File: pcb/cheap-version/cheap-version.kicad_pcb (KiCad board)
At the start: 4 copper layers, 100 x 100 mm, 169 parts, among them J201 UART / 3V3 logic, J301 SHT4x / XH 2.50, J302 FLOAT / 3.5 mm, J401 HRO TF-01A, J501 FAN1 / 3.5 mm, J511 FAN2 / 3.5 mm, J521 PUMP 24V / 6W, J601 PTC + / switched - (3.5 mm), J711 LED +/- (return isolated), J721 LED +/- (return isolated), J731 LED +/- (return isolated), J901 24V IN (KF301-5.0-2P), Q501 AO3400A, Q511 AO3400A, Q521 AO3422, Q601 IRL2505, Q711 BSC146N10LS5, Q721 BSC146N10LS5, SW201 RESET, SW202 BOOT, U101 ST1S10PHR, U201 ESP32-WROOM-32E-N4, U301 PCF8563T/5, U601 IRS4427S, U700 SN74LVC1G08DBVR, U710 AL8853S-13, U720 AL8853S-13, U902 ST1S14PHR, Y301 32.768k 12.5pF

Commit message: Complete cheap-version connections and load project routing rules
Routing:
- net +24V_LOADS: track 54.0 -> 74.8 mm, vias 0 -> 2
- net /LEDDrivers/LED2_OUT: track 87.8 -> 102.1 mm, vias 1 -> 3
- net +3V3: track 226.9 -> 238.9 mm, vias 2 -> 4
- net /LEDDrivers/LED2_GATE: track 1.78 -> 12.2 mm
- net /LEDDrivers/LED1_RETURN: track 0.00 -> 8.91 mm
- net /InputPower/AUX_VIN: track 37.8 -> 44.7 mm, vias 3 -> 5
- net /LEDDrivers/LED1_GATE: track 2.35 -> 8.55 mm, vias 0 -> 2
- net /LEDDrivers/LED2_OVP: track 6.29 -> 9.98 mm, vias 0 -> 2
- added copper zone on In2.Cu, net +3V3
- added copper zone on B.Cu, net GND
- added copper zone on F.Cu, net GND

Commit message: Reinforce cheap-version input and heater copper
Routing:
- net +24V_LOADS: track 74.8 -> 22.7 mm
- net GND: vias 99 -> 103
- added copper zone on B.Cu, net +24V
- added copper zone on F.Cu, net +24V
- added copper zone on B.Cu, net +24V_LOADS
- added copper zone on B.Cu, net /Outputs/Heater/HEATER_DRAIN
- added copper zone on F.Cu, net /Outputs/Heater/HEATER_DRAIN
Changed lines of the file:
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@@
 			(roundrect_rratio 0.032051)
 			(net "+24V")
+			(zone_connect 2)
 		)
 		(pad "2" smd roundrect
@@
 			(roundrect_rratio 0.104167)
 			(net "+24V_LOADS")
+			(zone_connect 2)
 		)
 		(pad "2" thru_hole circle
@@
 			(remove_unused_layers no)
 			(net "/Outputs/Heater/HEATER_DRAIN")
+			(zone_connect 2)
 		)
 		(embedded_fonts no)
@@
 			(roundrect_rratio 0.25)
 			(net "+24V")
+			(zone_connect 2)
 		)
 		(pad "1" thru_hole circle
@@
 			(remove_unused_layers no)
 			(net "+24V")
+			(zone_connect 2)
 		)
 		(pad "2" thru_hole circle
@@
 			(remove_unused_layers no)
 			(net "+24V_LOADS")
+			(zone_connect 2)
 		)
 		(pad "2" thru_hole circle
@@
 			(remove_unused_layers no)
 			(net "+24V_LOADS")
+			(zone_connect 2)
 		)
 		(embedded_fonts no)
@@
 	)
 	(via
+		(at 61.5 82.5)
+		(size 0.8)
+		(drill 0.4)
+		(layers "F.Cu" "B.Cu")
+		(locked yes)
+		(net "GND")
+	)
+	(via
 		(at 80.865 91.425)
 		(size 0.65)
@@
 	)
 	(via
+		(at 60.5 80.5)
+		(size 0.8)
+		(drill 0.4)
+		(layers "F.Cu" "B.Cu")
+		(locked yes)
+		(net "GND")
+	)
+	(via
 		(at 104.941267 118.220951)
 		(size 0.65)
@@
 	)
 	(via
+		(at 60.5 81.5)
+		(size 0.8)
+		(drill 0.4)
+		(layers "F.Cu" "B.Cu")
+		(locked yes)
+		(net "GND")
+	)
+	(via
 		(at 85.1125 80.25)
 		(size 0.65)
@@
 	)
 	(via
+		(at 60.5 82.5)
+		(size 0.8)
+		(drill 0.4)
+		(layers "F.Cu" "B.Cu")
+		(locked yes)
+		(net "GND")
+	)
+	(via
 		(at 131.174999 78.8)
 		(size 0.65)
@@
 	)
 	(segment
-		(start 61.1 82.9)
-		(end 60.8 82.6)
-		(width 1)
-		(locked yes)
-		(layer "B.Cu")
-		(net "+24V_LOADS")
-	)
-	(segment
-		(start 66.099999 82.9)
-		(end 61.1 82.9)
-		(width 1)
-		(locked yes)
-		(layer "B.Cu")
-		(net "+24V_LOADS")
-	)
-	(segment
-		(start 67.2 84)
-		(end 66.099999 82.9)
-		(width 1)
-		(locked yes)
-		(layer "B.Cu")
-		(net "+24V_LOADS")
-	)
-	(segment
-		(start 60.8 82.6)
-		(end 60.7 82.6)
+		(start 69.5 77)
+		(end 69.5 81.7)
 		(width 1)
 		(locked yes)
@@
 	)
 	(segment
-		(start 60.7 82.6)
-		(end 56.1 78)
+		(start 69.5 81.7)
+		(end 67.2 84)
 		(width 1)
 		(locked yes)
@@
 	)
 	(segment
-		(start 56.2589 75.8411)
-		(end 73.5589 75.8411)
-		(width 3)
-		(layer "In2.Cu")
-		(net "+24V_LOADS")
-	)
-	(segment
-		(start 89.65 59.75)
-		(end 89.65 56.35)
-		(width 3)
-		(layer "In2.Cu")
-		(net "+24V_LOADS")
-	)
-	(segment
-		(start 73.5589 75.8411)
-		(end 89.65 59.75)
-		(width 3)
-		(layer "In2.Cu")
-		(net "+24V_LOADS")
-	)
-	(segment
-		(start 54.1 78)
-		(end 56.2589 75.8411)
-		(width 3)
-		(layer "In2.Cu")
-		(net "+24V_LOADS")
-	)
-	(segment
 		(start 146.5 134.54)
 		(end 141.965 134.54)
@@
 	)
 	(zone
+		(net "+24V")
+		(layer "F.Cu")
+		(name "auto:input-stage:input top")
+		(hatch edge 0.5)
+		(priority 10)
+		(connect_pads yes
+			(clearance 0)
+		)
+		(min_thickness 0.25)
+		(fill yes
+			(thermal_gap 0.4)
+			(thermal_bridge_width 0.5)
+			(island_removal_mode 0)
+		)
+		(polygon
+			(pts
+				(xy 52 51) (xy 84 51) (xy 84 76) (xy 75 76) (xy 75 65) (xy 70.5 65) (xy 70.5 61) (xy 52 61)
+			)
+		)
+	)
+	(zone
 		(net "GND")
 		(layer "F.Cu")
@@
 	)
 	(zone
+		(net "/Outputs/Heater/HEATER_DRAIN")
+		(layer "F.Cu")
+		(name "auto:input-stage:heater top")
+		(hatch edge 0.5)
+		(priority 10)
+		(connect_pads yes
+			(clearance 0)
+		)
+		(min_thickness 0.25)
+		(fill yes
+			(thermal_gap 0.4)
+			(thermal_bridge_width 0.5)
+			(island_removal_mode 0)
+		)
+		(polygon
+			(pts
+				(xy 51.5 80) (xy 55.5 80) (xy 59.5 84) (xy 62 84) (xy 63.5 80) (xy 65.4 80) (xy 66.4 83) (xy 66.4 87.8)
+				(xy 58 87.8) (xy 51.5 82)
+			)
+		)
+	)
+	(zone
+		(net "/Outputs/Heater/HEATER_DRAIN")
+		(layer "B.Cu")
+		(name "auto:input-stage:heater bottom")
+		(hatch edge 0.5)
+		(priority 10)
+		(connect_pads yes
+			(clearance 0)
+		)
+		(min_thickness 0.25)
+		(fill yes
+			(thermal_gap 0.4)
+			(thermal_bridge_width 0.5)
+			(island_removal_mode 0)
+		)
+		(polygon
+			(pts
+				(xy 51.5 80) (xy 55.5 80) (xy 59.5 84) (xy 62 84) (xy 63.5 80) (xy 65.4 80) (xy 66.4 83) (xy 66.4 87.8)
+				(xy 58 87.8) (xy 51.5 82)
+			)
+		)
+	)
+	(zone
+		(net "+24V")
+		(layer "B.Cu")
+		(name "auto:input-stage:input bottom")
+		(hatch edge 0.5)
+		(priority 10)
+		(connect_pads yes
+			(clearance 0)
+		)
+		(min_thickness 0.25)
+		(fill yes
+			(thermal_gap 0.4)
+			(thermal_bridge_width 0.5)
+			(island_removal_mode 0)
+		)
+		(polygon
+			(pts
+				(xy 52 51) (xy 84 51) (xy 84 61.5) (xy 52 61.5)
+			)
+		)
+	)
+	(zone
 		(net "GND")
 		(layer "B.Cu")
@@
 			)
 		)
+	)
+	(zone
+		(net "+24V_LOADS")
+		(layer "B.Cu")
+		(name "auto:input-stage:loads bottom")
+		(hatch edge 0.5)
+		(priority 10)
+		(connect_pads yes
+			(clearance 0)
+		)
+		(min_thickness 0.25)
+		(fill yes
+			(thermal_gap 0.4)
+			(thermal_bridge_width 0.5)
+			(island_removal_mode 0)
+		)
+		(polygon
+			(pts
+				(xy 86.5 53) (xy 93 53) (xy 93 64) (xy 77.7 79.3) (xy 51.5 79.3) (xy 51.5 72.8) (xy 75 72.8) (xy 86.5 61.3)
+			)
+		)

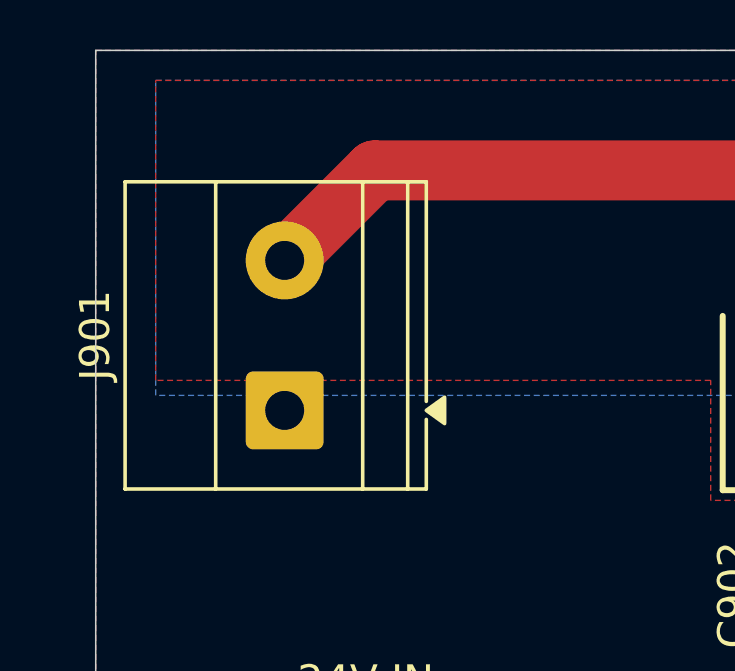
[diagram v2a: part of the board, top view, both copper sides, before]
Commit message: Turn 24V input terminal toward board edge preserving polarity
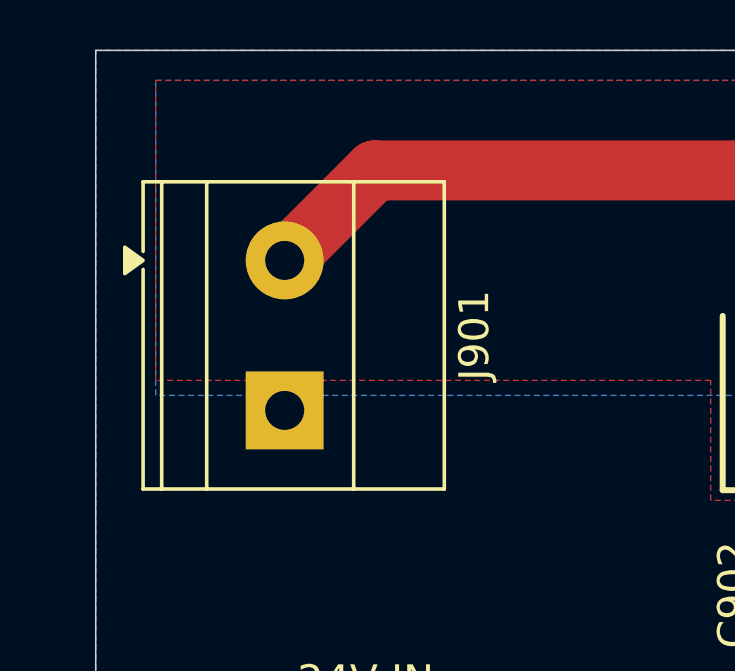
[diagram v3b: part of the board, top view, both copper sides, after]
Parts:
- J901: footprint TerminalBlock_Phoenix:TerminalBlock_Phoenix_MKDS-1,5-2_1x02_P5.00mm_Horizontal -> GrowBox:TerminalBlock_KF301_1x02_P5.00mm_Horizontal_Input
- moved J901 5.00 mm to (56.3, 57.0), turned to -90 degrees
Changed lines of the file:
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@@
 		)
 	)
-	(footprint "TerminalBlock_Phoenix:TerminalBlock_Phoenix_MKDS-1,5-2_1x02_P5.00mm_Horizontal"
+	(footprint "GrowBox:TerminalBlock_KF301_1x02_P5.00mm_Horizontal_Input"
 		(layer "F.Cu")
-		(at 56.3 62 90)
-		(descr "Terminal Block Phoenix MKDS-1,5-2, 2 pins, pitch 5mm, size 10x9.8mm, drill diameter 1.3mm, pad diameter 2.6mm, http://www.farnell.com/datasheets/100425.pdf")
+		(at 56.3 57 -90)
+		(descr "KF301 input; reversed numbering: 1 GND, 2 +24V; KiCad MKDS body surrogate")
 		(tags "THT Terminal Block Phoenix MKDS-1,5-2 pitch 5mm size 10x9.8mm drill 1.3mm pad 2.6mm")
 		(property "Reference" "J901"
-			(at 2.5 -6.32 90)
+			(at 2.5 -6.32 270)
 			(layer "F.SilkS")
 			(effects
@@
 		)
 		(property "Value" "24V IN (KF301-5.0-2P)"
-			(at 2.5 5.72 90)
+			(at 2.5 5.72 270)
 			(layer "F.Fab")
 			(effects
@@
 		)
 		(property "Datasheet" ""
-			(at 0 0 90)
+			(at 0 0 270)
 			(layer "F.Fab")
 			(hide yes)
@@
 		)
 		(property "Description" ""
-			(at 0 0 90)
+			(at 0 0 270)
 			(layer "F.Fab")
 			(hide yes)
@@
 		)
 		(property "KiLib_Generator" "terminal_block/Phoenix"
-			(at 0 0 90)
+			(at 0 0 270)
 			(layer "F.SilkS")
 			(hide yes)
@@
 		)
 		(property "MPN" "KF301-5.0-2P"
-			(at 0 0 0)
+			(at 0 0 180)
 			(layer "F.SilkS")
 			(hide yes)
@@
 		(duplicate_pad_numbers_are_jumpers no)
 		(fp_line
+			(start -2.62 4.72)
+			(end -2.62 -5.32)
+			(stroke
+				(width 0.12)
+				(type solid)
+			)
+			(layer "F.SilkS")
+		)
+		(fp_line
+			(start -0.3 4.72)
+			(end -2.62 4.72)
+			(stroke
+				(width 0.12)
+				(type solid)
+			)
+			(layer "F.SilkS")
+		)
+		(fp_line
+			(start 7.62 4.72)
+			(end 0.3 4.72)
+			(stroke
+				(width 0.12)
+				(type solid)
+			)
+			(layer "F.SilkS")
+		)
+		(fp_line
+			(start -2.62 4.1)
+			(end 7.62 4.1)
+			(stroke
+				(width 0.12)
+				(type solid)
+			)
+			(layer "F.SilkS")
+		)
+		(fp_line
+			(start -2.62 2.6)
+			(end 7.62 2.6)
+			(stroke
+				(width 0.12)
+				(type solid)
+			)
+			(layer "F.SilkS")
+		)
+		(fp_line
+			(start -2.62 -2.3)
+			(end 7.62 -2.3)
+			(stroke
+				(width 0.12)
+				(type solid)
+			)
+			(layer "F.SilkS")
+		)
+		(fp_line
+			(start -2.62 -5.32)
+			(end 7.62 -5.32)
+			(stroke
+				(width 0.12)
+				(type solid)
+			)
+			(layer "F.SilkS")
+		)
+		(fp_line
 			(start 7.62 -5.32)
 			(end 7.62 4.72)
-			(stroke
-				(width 0.12)
-				(type solid)
-			)
-			(layer "F.SilkS")
-		)
-		(fp_line
-			(start -2.62 -5.32)
-			(end 7.62 -5.32)
-			(stroke
-				(width 0.12)
-				(type solid)
-			)
-			(layer "F.SilkS")
-		)
-		(fp_line
-			(start -2.62 -2.3)
-			(end 7.62 -2.3)
-			(stroke
-				(width 0.12)
-				(type solid)
-			)
-			(layer "F.SilkS")
-		)
-		(fp_line
-			(start -2.62 2.6)
-			(end 7.62 2.6)
-			(stroke
-				(width 0.12)
-				(type solid)
-			)
-			(layer "F.SilkS")
-		)
-		(fp_line
-			(start -2.62 4.1)
-			(end 7.62 4.1)
-			(stroke
-				(width 0.12)
-				(type solid)
-			)
-			(layer "F.SilkS")
-		)
-		(fp_line
-			(start 7.62 4.72)
-			(end 0.3 4.72)
-			(stroke
-				(width 0.12)
-				(type solid)
-			)
-			(layer "F.SilkS")
-		)
-		(fp_line
-			(start -0.3 4.72)
-			(end -2.62 4.72)
-			(stroke
-				(width 0.12)
-				(type solid)
-			)
-			(layer "F.SilkS")
-		)
-		(fp_line
-			(start -2.62 4.72)
-			(end -2.62 -5.32)
 			(stroke
 				(width 0.12)
@@
 		)
 		(fp_line
+			(start -2 4.6)
+			(end -2.5 4.1)
+			(stroke
+				(width 0.1)
+				(type solid)
+			)
+			(layer "F.Fab")
+		)
+		(fp_line
+			(start 7.5 4.6)
+			(end -2 4.6)
+			(stroke
+				(width 0.1)
+				(type solid)
+			)
+			(layer "F.Fab")
+		)
+		(fp_line
+			(start -2.5 4.1)
+			(end 7.5 4.1)
+			(stroke
+				(width 0.1)
+				(type solid)
+			)
+			(layer "F.Fab")
+		)
+		(fp_line
+			(start -2.5 4.1)
+			(end -2.5 -5.2)
+			(stroke
+				(width 0.1)
+				(type solid)
+			)
+			(layer "F.Fab")
+		)
+		(fp_line
+			(start -2.5 2.6)
+			(end 7.5 2.6)
+			(stroke
+				(width 0.1)
+				(type solid)
+			)
+			(layer "F.Fab")
+		)
+		(fp_line
+			(start 1.138 -0.955)
+			(end -0.955 1.138)
+			(stroke
+				(width 0.1)
+				(type solid)
+			)
+			(layer "F.Fab")
+		)
+		(fp_line
+			(start 6.138 -0.955)
+			(end 4.045 1.138)
+			(stroke
+				(width 0.1)
+				(type solid)
+			)
+			(layer "F.Fab")
+		)
+		(fp_line
+			(start 0.955 -1.138)
+			(end -1.138 0.955)
+			(stroke
+				(width 0.1)
+				(type solid)
+			)
+			(layer "F.Fab")
+		)
+		(fp_line
+			(start 5.955 -1.138)
+			(end 3.862 0.955)
+			(stroke
+				(width 0.1)
+				(type solid)
+			)
+			(layer "F.Fab")
+		)
+		(fp_line
+			(start -2.5 -2.3)
+			(end 7.5 -2.3)
+			(stroke
+				(width 0.1)
+				(type solid)
+			)
+			(layer "F.Fab")
+		)
+		(fp_line
+			(start -2.5 -5.2)
+			(end 7.5 -5.2)
+			(stroke
+				(width 0.1)
+				(type solid)
+			)
+			(layer "F.Fab")
+		)
+		(fp_line
 			(start 7.5 -5.2)
 			(end 7.5 4.6)
@@
 			(layer "F.Fab")
 		)
-		(fp_line
-			(start -2.5 -5.2)
-			(end 7.5 -5.2)
-			(stroke
-				(width 0.1)
-				(type solid)
-			)
-			(layer "F.Fab")
-		)
-		(fp_line
-			(start -2.5 -2.3)
-			(end 7.5 -2.3)
-			(stroke
-				(width 0.1)
-				(type solid)
-			)
-			(layer "F.Fab")
-		)
-		(fp_line
-			(start 5.955 -1.138)
-			(end 3.862 0.955)
-			(stroke
-				(width 0.1)
-				(type solid)
-			)
-			(layer "F.Fab")
-		)
-		(fp_line
-			(start 0.955 -1.138)
-			(end -1.138 0.955)
-			(stroke
-				(width 0.1)
-				(type solid)
-			)
-			(layer "F.Fab")
-		)
-		(fp_line
-			(start 6.138 -0.955)
-			(end 4.045 1.138)
-			(stroke
-				(width 0.1)
-				(type solid)
-			)
-			(layer "F.Fab")
-		)
-		(fp_line
-			(start 1.138 -0.955)
-			(end -0.955 1.138)
-			(stroke
-				(width 0.1)
-				(type solid)
-			)
-			(layer "F.Fab")
-		)
-		(fp_line
-			(start -2.5 2.6)
-			(end 7.5 2.6)
-			(stroke
-				(width 0.1)
-				(type solid)
-			)
-			(layer "F.Fab")
-		)
-		(fp_line
-			(start -2.5 4.1)
-			(end -2.5 -5.2)
-			(stroke
-				(width 0.1)
-				(type solid)
-			)
-			(layer "F.Fab")
-		)
-		(fp_line
-			(start -2.5 4.1)
-			(end 7.5 4.1)
-			(stroke
-				(width 0.1)
-				(type solid)
-			)
-			(layer "F.Fab")
-		)
-		(fp_line
-			(start 7.5 4.6)
-			(end -2 4.6)
-			(stroke
-				(width 0.1)
-				(type solid)
-			)
-			(layer "F.Fab")
-		)
-		(fp_line
-			(start -2 4.6)
-			(end -2.5 4.1)
-			(stroke
-				(width 0.1)
-				(type solid)
-			)
+		(fp_circle
+			(center 0 0)
+			(end 1.5 0)
+			(stroke
+				(width 0.1)
+				(type solid)
+			)
+			(fill no)
 			(layer "F.Fab")
 		)
@@
 			(layer "F.Fab")
 		)
-		(fp_circle
-			(center 0 0)
-			(end 1.5 0)
-			(stroke
-				(width 0.1)
-				(type solid)
-			)
-			(fill no)
-			(layer "F.Fab")
-		)
 		(fp_text user "${REFERENCE}"
-			(at 2.5 3.2 90)
+			(at 2.5 3.2 270)
 			(layer "F.Fab")
 			(effects
@@
 			)
 		)
-		(pad "1" thru_hole roundrect
-			(at 0 0 90)
+		(pad "1" thru_hole rect
+			(at 5 0 270)
 			(size 2.6 2.6)
 			(drill 1.3)
 			(layers "*.Cu" "*.Mask")
 			(remove_unused_layers no)
-			(roundrect_rratio 0.096154)
 			(net "GND")
 			(zone_connect 2)
+			(thermal_bridge_angle 45)
 		)
 		(pad "2" thru_hole circle
-			(at 5 0 90)
+			(at 0 0 270)
 			(size 2.6 2.6)
 			(drill 1.3)
@@
 			(net "+24V")
 			(zone_connect 2)
+			(thermal_bridge_angle 90)
 		)
 		(embedded_fonts no)
